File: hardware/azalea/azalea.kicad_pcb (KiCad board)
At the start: 4 copper layers, 70.7 x 53.3 mm, 88 parts, among them J1 NEIGHBOR1, J2 NEIGHBOR2, J3 USB-MICRO-B-SHIELDED, J4 USB-MICRO-B-SHIELDED, J5 JTAG, J7 BONUS_ROW, SW1 DFU, SW2 RESET, U1 LPC4330FBD144, U2 W25Q16DV, U3 AP7333, U4 IP4220CZ6, U5 NX5P2553GV, X1 XTAL4PIN, X2 RTC_XTAL

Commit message: azalea: finished first pass at routing
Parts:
- moved R12 2.14 mm to (125.0, 109.2), turned to 90 degrees
- moved C3 0.76 mm to (115.6, 85.6)
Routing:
- net /RESET: track 16.5 -> 113.6 mm, vias 1 -> 4
- net /P2_8: track 41.8 -> 84.3 mm, vias 1 -> 3
- net /LED3: track 42.0 -> 62.6 mm, vias 2 -> 4
- net /TDI: track 0.00 -> 20.1 mm, vias 0 -> 1
- net /TCK: track 0.00 -> 18.3 mm
- net /TMS: track 0.00 -> 17.9 mm, vias 0 -> 1
- net /DBGEN: track 0.00 -> 14.6 mm
- net /TDO: track 0.00 -> 14.1 mm
- net VCC: track 63.8 -> 76.9 mm, vias 19 -> 27
- net /TRST: track 0.00 -> 10.2 mm
- net /LED4: track 49.7 -> 57.3 mm, vias 2 -> 4
- net GND: track 68.5 -> 73.6 mm, vias 43 -> 47
- net /LED1: track 31.0 -> 35.2 mm
- net /LED2: track 22.1 -> 25.8 mm
- net Net-(D1-Pad2): track 0.00 -> 3.43 mm
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- added copper zone on B.Cu, net /VBUS

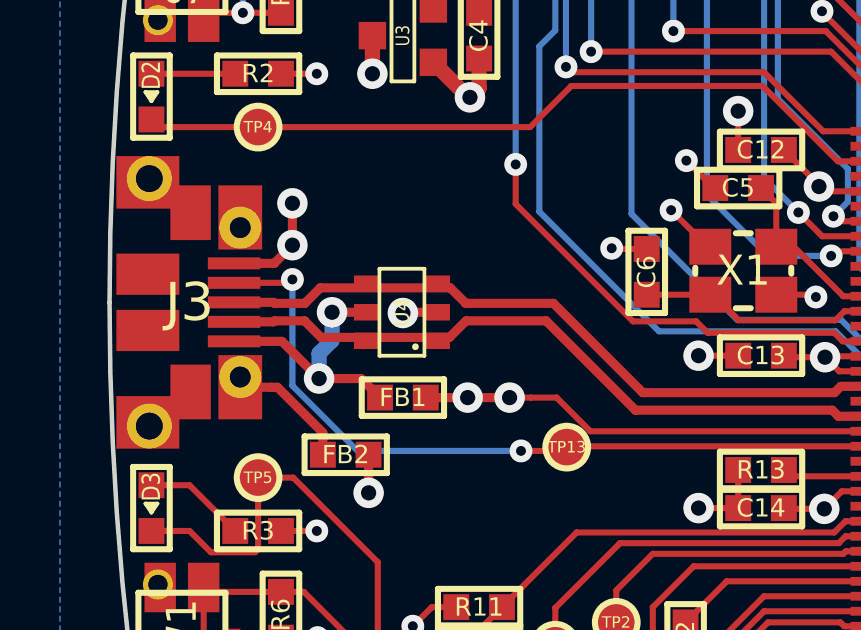
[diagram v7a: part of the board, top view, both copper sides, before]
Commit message: azalea: reoriented ESD diode, added USB0_ID protection
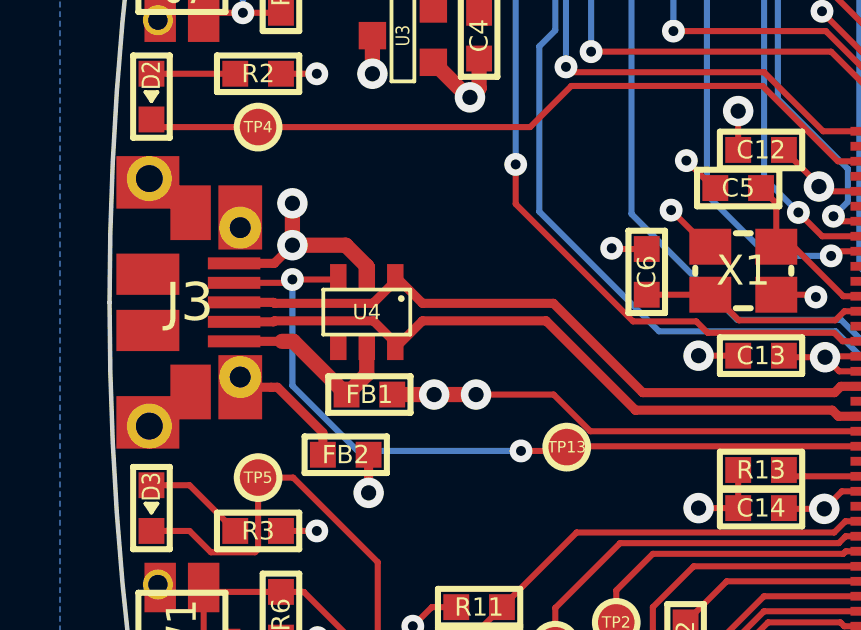
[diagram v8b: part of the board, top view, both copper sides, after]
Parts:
- moved U4 1.17 mm to (114.4, 98.1), turned to 180 degrees
- moved FB1 1.12 mm to (114.5, 100.9)
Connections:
- U4 pad 1: /USB0_D- -> /USB0_D+
- U4 pad 3: /USB0_D+ -> /USB0_ID
- U4 pad 4: /USB0_D+ -> Net-(U4-Pad4)
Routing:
- net Net-(FB1-Pad1): track 9.47 -> 6.31 mm, vias 2 -> 0
- net GND: track 73.6 -> 75.5 mm, vias 47 -> 46
- net /USB0_ID: track 25.8 -> 27.4 mm
- net /VBUS: track 20.9 -> 22.0 mm
